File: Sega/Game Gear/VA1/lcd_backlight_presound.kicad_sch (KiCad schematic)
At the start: 1 part

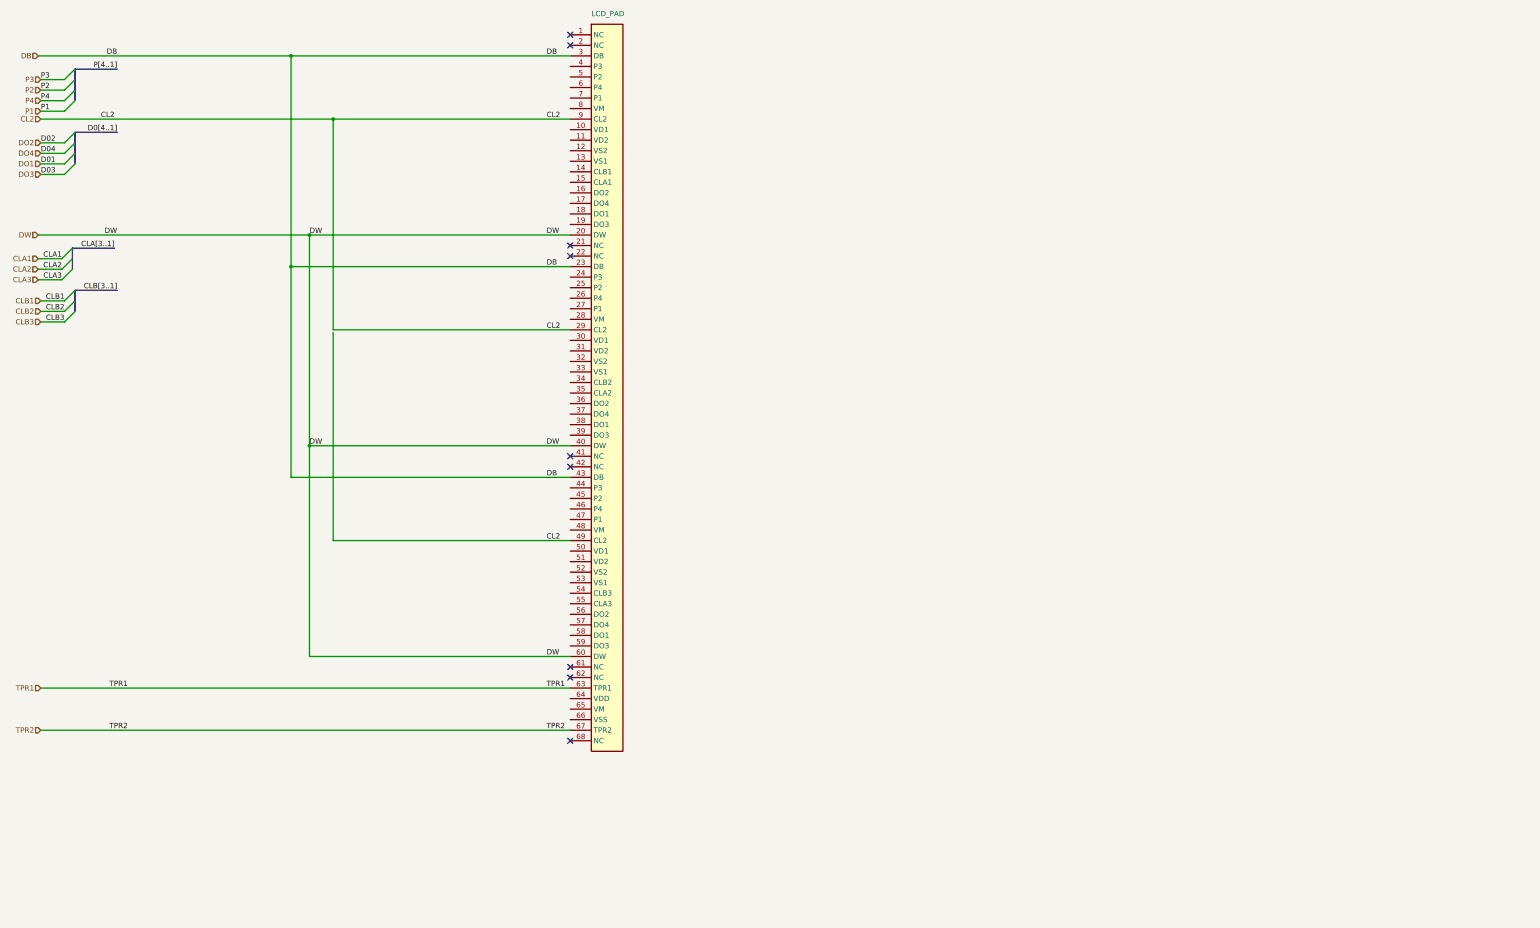
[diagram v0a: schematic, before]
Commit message: Prepping for sound pre-amp to be added to LCD sheet
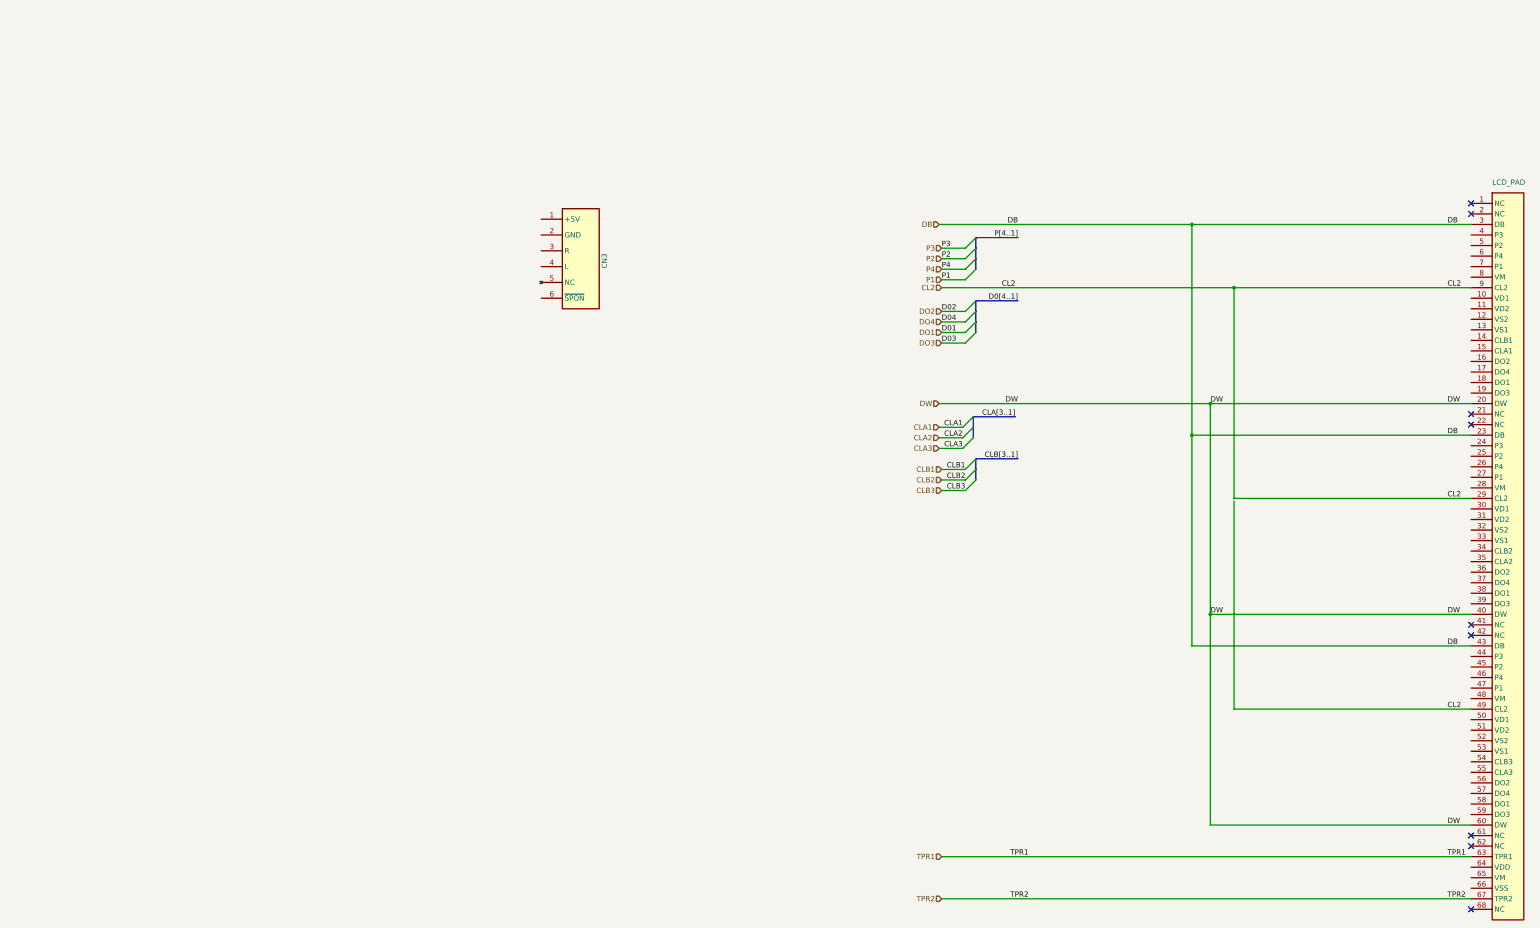
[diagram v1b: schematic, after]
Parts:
- added CN3: ~, symbol Game Gear Symbol Library:Wire_6P_GG
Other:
- moved on the sheet: LCD_PAD

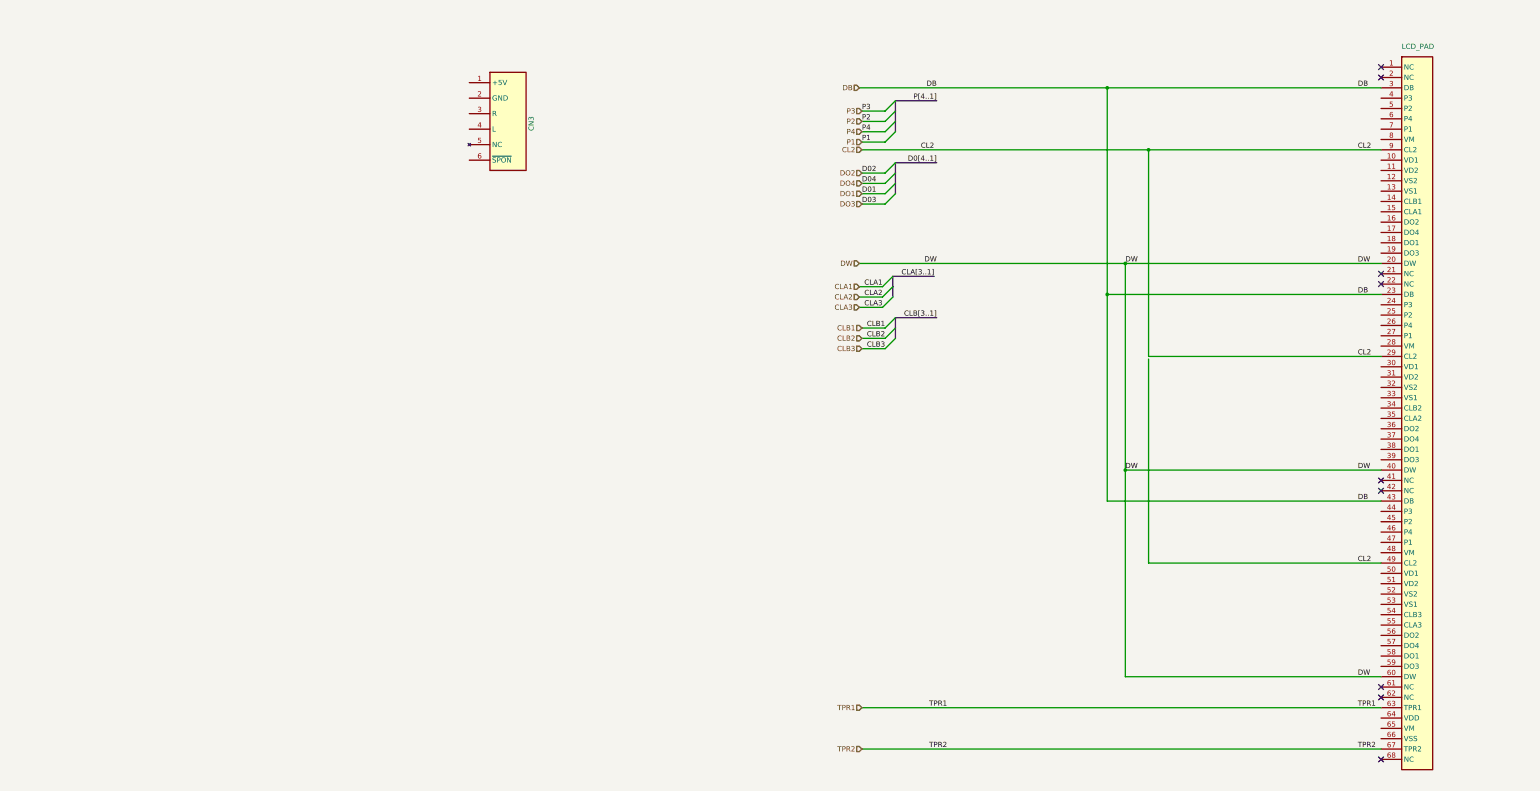
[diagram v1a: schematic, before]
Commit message: Routed sound to LCD, created SND bus alias, created tv_sound alias, fixed issue where control and data intersected, changed serial conn to passive, finished minor signals on top of asic, power conn area, and started lcd routing.
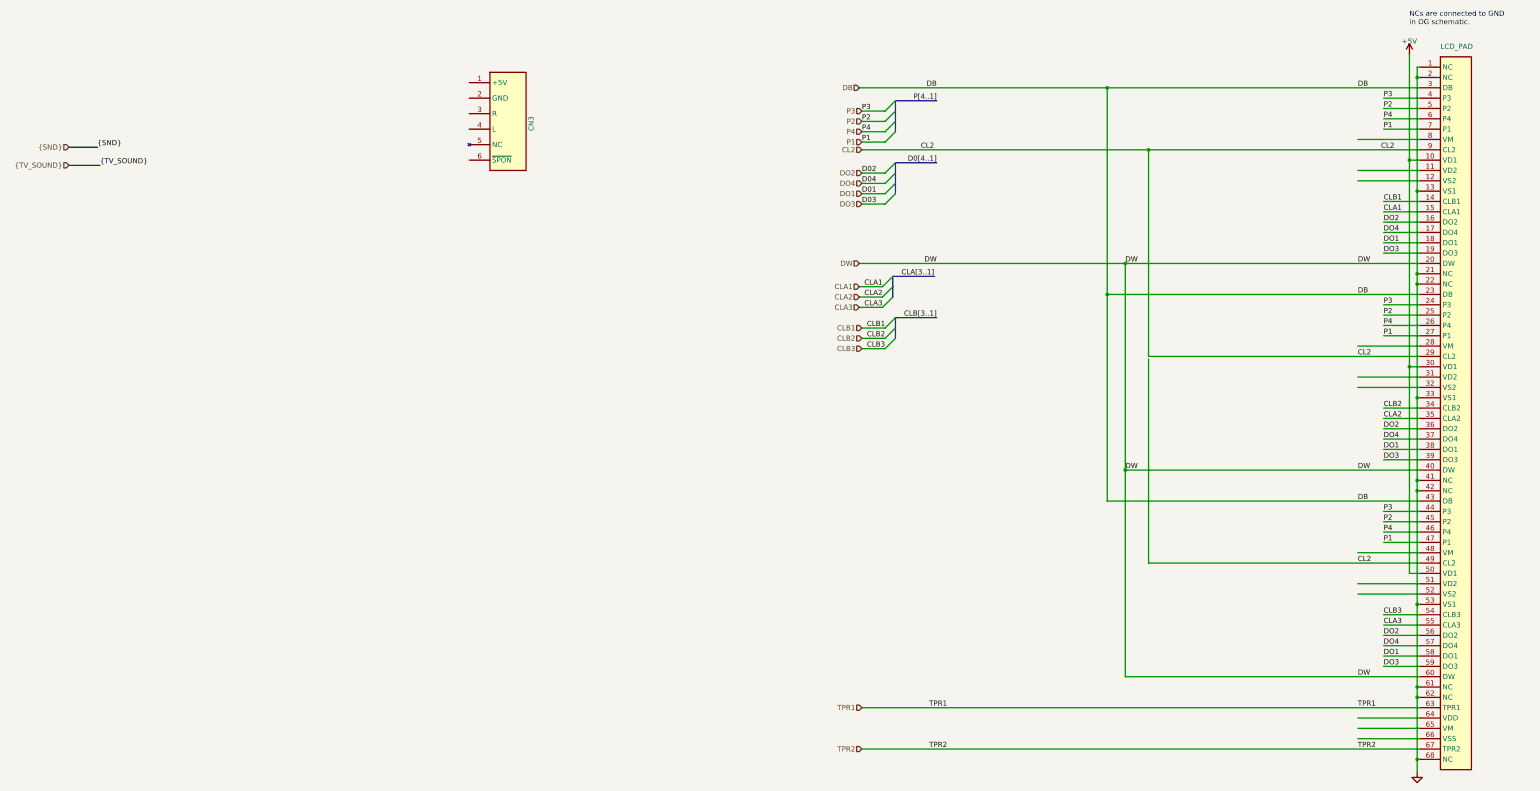
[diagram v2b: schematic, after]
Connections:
- net CLA1: now also LCD_PAD.15 (CLA1)
- net CLA2: now also LCD_PAD.35 (CLA2)
- net CLA3: now also LCD_PAD.55 (CLA3)
- net CLB1: now also LCD_PAD.14 (CLB1)
- net CLB2: now also LCD_PAD.34 (CLB2)
- net CLB3: now also LCD_PAD.54 (CLB3)
- net DO1: now also LCD_PAD.18 (DO1), LCD_PAD.38 (DO1), LCD_PAD.58 (DO1)
- net DO2: now also LCD_PAD.16 (DO2), LCD_PAD.36 (DO2), LCD_PAD.56 (DO2)
- net DO3: now also LCD_PAD.19 (DO3), LCD_PAD.39 (DO3), LCD_PAD.59 (DO3)
- net DO4: now also LCD_PAD.17 (DO4), LCD_PAD.37 (DO4), LCD_PAD.57 (DO4)
- net P1: now also LCD_PAD.27 (P1), LCD_PAD.47 (P1), LCD_PAD.7 (P1)
- net P2: now also LCD_PAD.25 (P2), LCD_PAD.45 (P2), LCD_PAD.5 (P2)
- net P3: now also LCD_PAD.24 (P3), LCD_PAD.4 (P3), LCD_PAD.44 (P3)
- net P4: now also LCD_PAD.26 (P4), LCD_PAD.46 (P4), LCD_PAD.6 (P4)
- net GND: now reaches LCD_PAD.1 (NC)
- net GND: now also LCD_PAD.13 (VS1), LCD_PAD.2 (NC), LCD_PAD.21 (NC), LCD_PAD.22 (NC), LCD_PAD.33 (VS1), LCD_PAD.41 (NC), LCD_PAD.42 (NC), LCD_PAD.53 (VS1), LCD_PAD.61 (NC), LCD_PAD.62 (NC), LCD_PAD.68 (NC)
- net +5V: now reaches LCD_PAD.10 (VD1)
- net +5V: now also LCD_PAD.30 (VD1), LCD_PAD.50 (VD1)
- no-connect marks 9 -> 0
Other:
- note added: "NCs are connected to GND in OG schematic."
- moved on the sheet: LCD_PAD

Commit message: Message anlaog stuff in LCD section. 100% right. Yup. It is. Except for the mistakes.
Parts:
- added C44, C46, C48, C50, C59, C61: 100n, symbol Device:C_Small
- added C45: 4u7/35v, symbol Device:C_Polarized_Small
- added C47: 68u, symbol Device:C_Polarized_Small
- added C49: 100u, symbol Device:C_Polarized_Small
- added C58, C60: 470n, symbol Device:C_Small
- added C62, C63: 10n, symbol Device:C_Small
- added C64, C65: 470n/50v, symbol Device:C_Polarized_Small
- added C67, C68: 47p, symbol Device:C_Small
- added D1: 1ss184, symbol Game Gear Symbol Library:D_Dual_CommonCathode_AAK_90deg
- added D2, D3: 1ss184, symbol Device:D_Small_Filled
- added Q10, Q8: 2sa812, symbol Device:Q_PNP_BEC
- added Q11, Q5, Q6, Q7, Q9: 2sc1623, symbol Device:Q_NPN_BEC
- added R31, R32, R34: 100k, symbol Device:R_Small
- added R33: 30k, symbol Device:R_Small
- added R35: 31, symbol Device:R_Small
- added R36: 35k (1%), symbol Device:R_Small
- added R37: 30k (1%), symbol Device:R_Small
- added R38: 51, symbol Device:R_Small
- added R39, R40: 470 (1%), symbol Device:R_Small
- added R41: 2k2, symbol Device:R_Small
- added R42: 240k, symbol Device:R_Small
- added R43, R44, R46, R47: 22k, symbol Device:R_Small
- added R45: 1M, symbol Device:R_Small
- added VR1: 20k, symbol Device:R_Potentiometer_Small
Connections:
- net +5V: now also R38.2
- net GND: now also C44.2, C45.2, C61.2, D1.3 (A), Q5.2 (E), Q9.2 (E), R34.1
- net TPR1: now also R44.1; no longer LCD_PAD.63 (TPR1)
- net TPR2: now also R43.2; no longer LCD_PAD.67 (TPR2)
- net VD2: now reaches LCD_PAD.11 (VD2)
- net VD2: now also LCD_PAD.31 (VD2), LCD_PAD.51 (VD2), C47.1, C48.1, C58.1, C59.1, D2.2 (A), Q7.2 (E), R39.2
- net VS2: now reaches LCD_PAD.12 (VS2)
- net VS2: now also LCD_PAD.32 (VS2), LCD_PAD.52 (VS2), C47.2, C48.2, C49.2, C50.2, C58.2, C59.2, C60.2, D1.2 (K), D3.1 (K), R40.1
- net VM: now reaches LCD_PAD.28 (VM)
- net VM: now also LCD_PAD.48 (VM), LCD_PAD.65 (VM), LCD_PAD.8 (VM), C49.1, C50.1, C60.1, Q10.2 (E), Q11.2 (E), R39.1, R40.2
- net VDD: now reaches LCD_PAD.64 (VDD)
- net VDD: now also C64.1, C67.1, D2.1 (K), R45.2, R47.2
- net VSS: now reaches LCD_PAD.66 (VSS)
- net VSS: now also C65.2, C68.1, D3.2 (A), R45.1, R46.2
- new net: C63.2, Q9.1 (B), R42.1
- new net: C62.2, Q8.1 (B), R42.2
- new net: C46.1, Q7.1 (B), R36.1, R37.2
- new net: C46.2, D1.3 (A)
- new net: D1.1 (K), R37.1
- new net: C64.2, C65.1, Q8.3 (C), Q9.3 (C)
- new net: R34.2, VR1.3
- new net: Q5.1 (B), R31.2
- new net: Q5.3 (C), R32.2
- new net: Q10.1 (B), R43.1
- new net: C45.1, C61.1, Q8.2 (E), R35.1, R36.2
- new net: Q6.2 (E), R35.2
- new net: C62.1, C63.1, R41.1
- new net: Q11.1 (B), R44.2
- new net: R32.1, R33.1, VR1.1
- new net: C44.1, Q6.1 (B), VR1.2
- new net: Q7.3 (C), R38.1
- new net +34V: Q6.3 (C), R33.2
- new net A: R41.2
- new net TPR1*: C67.2, LCD_PAD.63 (TPR1), Q11.3 (C), R47.1
- new net TPR2*: C68.2, LCD_PAD.67 (TPR2), Q10.3 (C), R46.1
- new net ~{GG}: R31.1
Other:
- note added: "2c1623 SOT is B-E-C based on MCC datasheet"
- note added: "D1 is a AAK dual-diode"
- note added: "Hard to read values: R35 R36 R38"
- moved on the sheet: CN3

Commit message: lcd pcb connector wired up (wow!)
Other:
- note added: "D1 is a AAK dual-diode D2 and D3 are same part number, but appear to only be using one diode in each."
- note removed: "D1 is a AAK dual-diode"
- moved on the sheet: C44, C45, C46, C47, C48, C49, C50, C58, C59, C60, C61, C62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

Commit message: inverter, audio buffer, and cleaned up various signals. A group of terms and fitlers for LCD need to be added.
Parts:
- added C61, C62, C64, C67: 1u (Tant), symbol Device:C_Polarized_Small
- added C63: 100n, symbol Device:C_Small
- added C65, C66: 8200p, symbol Device:C_Small
- added C68: 100u, symbol Device:C_Polarized_Small
- added C69: 100n/50V (MP), symbol Device:C_Small
- added C70: 270p/2kV, symbol Device:C_Small
- added C71, C72: 22n, symbol Device:C_Small
- added FL1: ~, symbol Game Gear Symbol Library:CFL
- added FU1, FU2: Fuse, symbol Device:Fuse
- added IC4: uPC356, symbol Device:Opamp_Dual
- added L2: 105u, symbol Device:L_Small
- added M5 (x4): TestPoint_Small, symbol Connector:TestPoint_Small
- added Q3, Q4: 2sd1614, symbol Device:Q_NPN_BCE
- added R48, R49: 10k, symbol Device:R_Small
- added R50, R51: 47k, symbol Device:R_Small
- added R52, R53, R54, R55: 1k, symbol Device:R_Small
- added R56, R57: 1k8, symbol Device:R_Small
- added T1: Transformer_GG, symbol Game Gear Symbol Library:Transformer_LCD_CFL
- renumbered C61 to C51, C62 to C52, C63 to C53, C64 to C54, C65 to C55, C68 to C56, C67 to C57
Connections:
- net GND: now also CN3.2 (GND), C63.2, C65.2, C66.2, C71.2, IC4.4 (V-), R48.2, R49.2
- net +5VA: now reaches CN3.1 (+5V)
- net +5VA: now also C63.1, IC4.8 (V+)
- net at CN3.3 (R): now also C64.2, M5.1
- net at CN3.4 (L): now also C67.2, M5.1
- net ~{SPON}: now reaches CN3.6 (~{SPON})
- new net: C71.1, FU2.1, T1.6 (S1)
- new net: FL1.2, FU2.2, M5.1
- new net: C66.1, C67.1, R54.1, R55.1
- new net: C62.1, R55.2
- new net: L2.1, R56.2, R57.2
- new net: C72.1, L2.2, T1.2 (PM)
- new net: Q3.1 (B), R56.1, T1.5 (P5)
- new net: C69.1, Q3.2 (C), T1.1 (PR1)
- new net: C64.1, C65.1, R52.1, R53.1
- new net: FL1.1, FU1.2, M5.1
- new net: IC4.6 (-), IC4.7, R54.2
- new net: C70.1, T1.7 (S2)
- new net: C70.2, FU1.1
- new net: C61.1, R53.2
- new net: IC4.1, IC4.2 (-), R52.2
- new net: C69.2, Q4.2 (C), T1.3 (PR2)
- new net: Q4.1 (B), R57.1, T1.4 (P4)
- new net +2.5VA: R50.2, R51.2
- new net +5V_INVERT: C68.1
- new net Invert: C68.2, C72.2, Q3.3 (E), Q4.3 (E)
- new net SNDL: IC4.5 (+), R51.1
- new net SNDR: IC4.3 (+), R50.1
- new net TVSNDL: C62.2, R48.1
- new net TVSNDR: C61.2, R49.1
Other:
- moved on the sheet: CN3
